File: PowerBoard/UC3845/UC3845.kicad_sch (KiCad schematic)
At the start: 41 parts, among them J1 AuxConn, J1 POWER_SW, Q1 STD11N65M2, U2 LT8316EFE#PBF

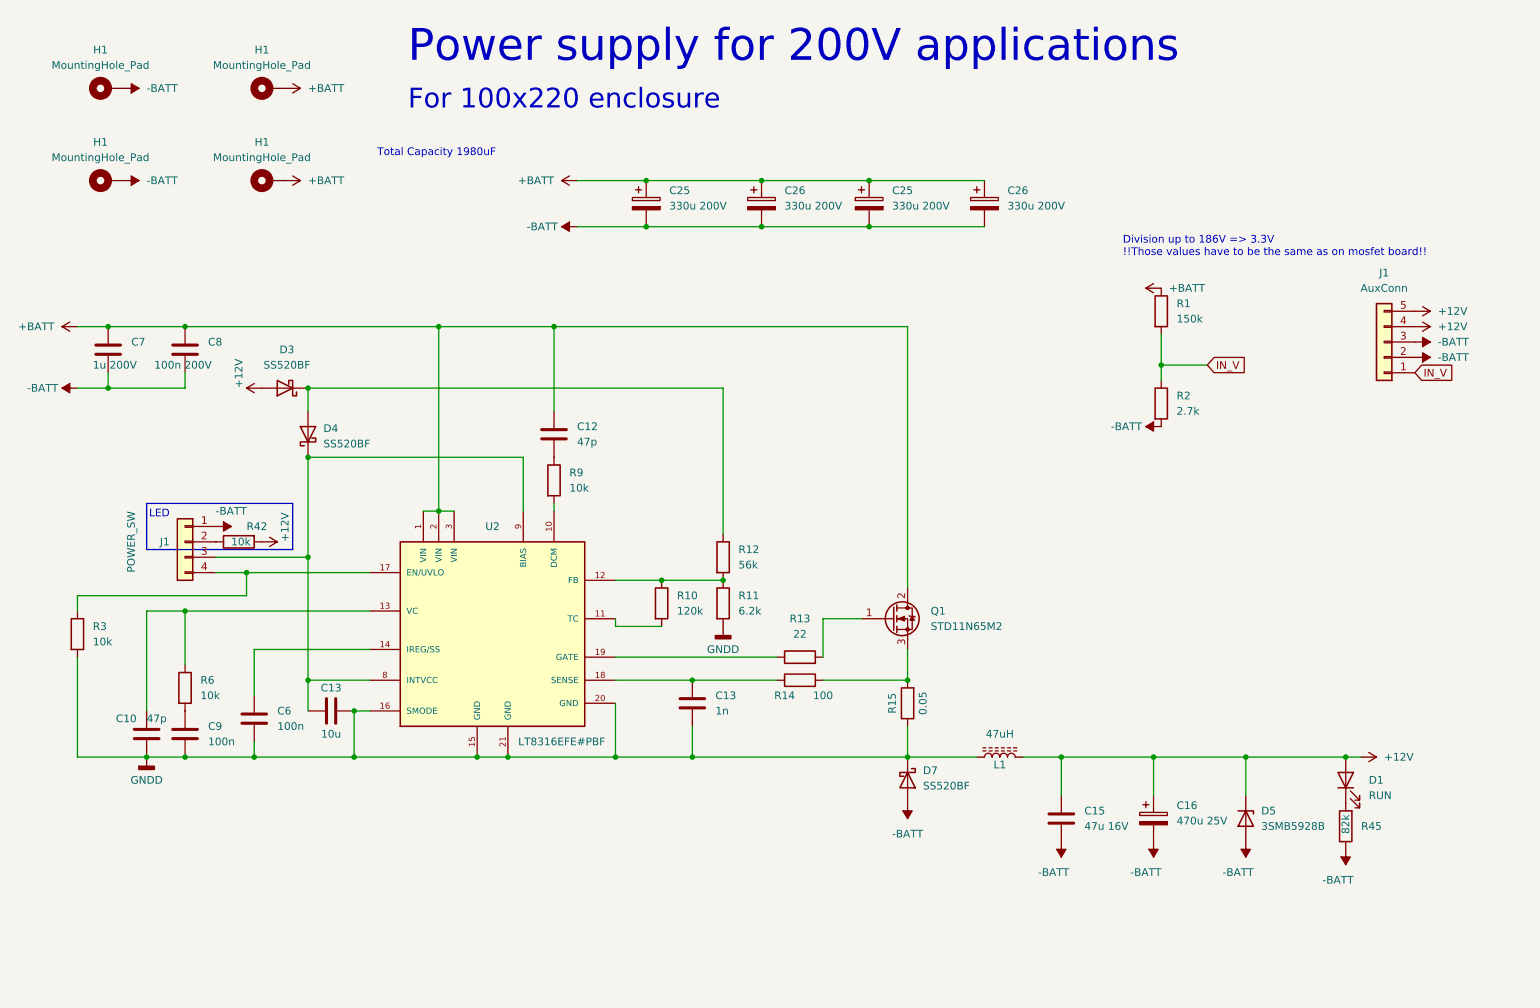
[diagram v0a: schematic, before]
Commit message: v3.0.1 - GaN redesign
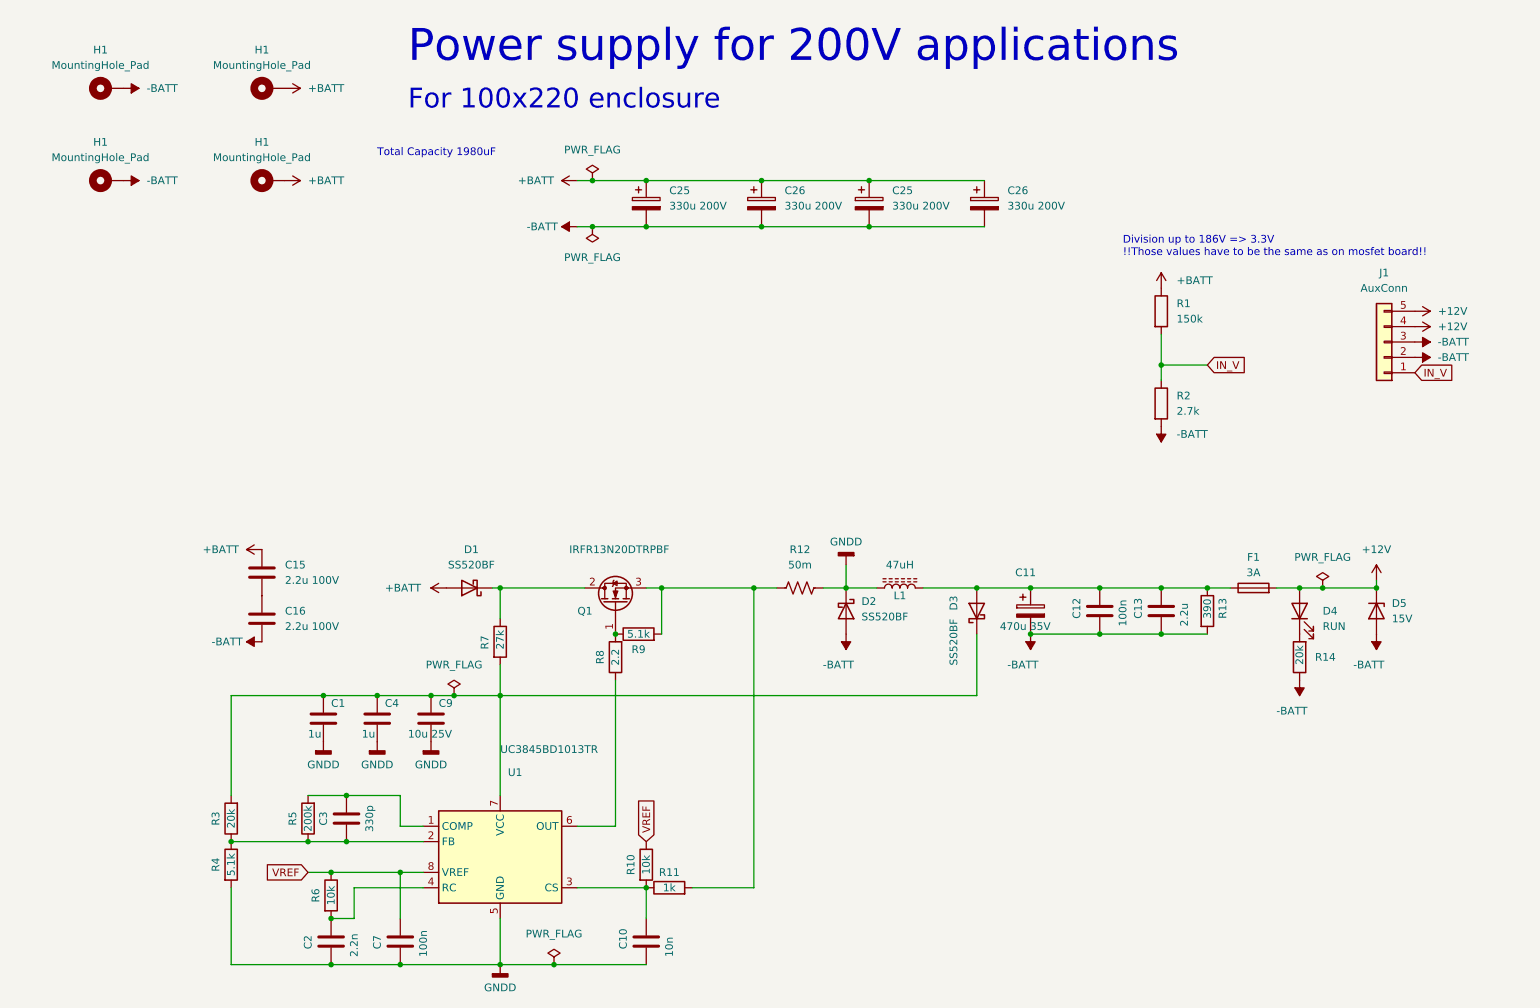
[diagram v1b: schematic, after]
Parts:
- removed C13: 1n, Capacitor_SMD:C_0603_1608Metric, symbol Device:C
- removed C13: 10u, Capacitor_SMD:C_0603_1608Metric, symbol Device:C
- removed C16: 470u 25V, Capacitor_SMD:CP_Elec_10x10.5, symbol Device:C_Polarized
- removed C6: 100n, GigaVescLibs:C_0603_1608Metric_L, symbol Device:C
- removed C8: 100n 200V, Capacitor_SMD:C_1206_3216Metric, symbol Device:C
- removed D1: RUN, Diode_SMD:D_0603_1608Metric, symbol Device:LED
- removed D4, D7: SS520BF, Diode_SMD:D_SMB, symbol Device:D_Schottky
- removed J1: POWER_SW, Connector_JST:JST_PH_B4B-PH-K_1x04_P2.00mm_Vertical, symbol Connector_Generic:Conn_01x04
- removed R12: 56k, Resistor_SMD:R_0603_1608Metric, symbol Device:R
- removed R15: 0.05, Resistor_SMD:R_2512_6332Metric, symbol Device:R
- removed R42: 10k, Resistor_SMD:R_0603_1608Metric, symbol Device:R
- removed R45: 82k, Resistor_SMD:R_0603_1608Metric, symbol Device:R
- removed U2: LT8316EFE#PBF, GigaVescLibs:IC_LT8316EFE#PBF, symbol GigaESCSymbols:LT8316EFE#PBF
- added C1, C4: 1u, Capacitor_SMD:C_0603_1608Metric, symbol Device:C
- added C11: 470u 35V, Capacitor_SMD:CP_Elec_10x10, symbol Device:C_Polarized
- added C13: 2.2u, Capacitor_SMD:C_0805_2012Metric, symbol Device:C
- added C16: 2.2u 100V, Capacitor_SMD:C_1206_3216Metric, symbol Device:C
- added C2: 2.2n, Capacitor_SMD:C_0603_1608Metric, symbol Device:C
- added C3: 330p, Capacitor_SMD:C_0603_1608Metric, symbol Device:C
- added D1, D2: SS520BF, Diode_SMD:D_SMB, symbol Device:D_Schottky
- added D4: RUN, Diode_SMD:D_0603_1608Metric, symbol Device:LED
- added F1: 3A, Fuse:Fuse_1206_3216Metric, symbol Device:Fuse
- added R12: 50m, Resistor_SMD:R_2512_6332Metric, symbol Device:R_US
- added R4: 5.1k, Resistor_SMD:R_0603_1608Metric, symbol Device:R
- added R5: 200k, Resistor_SMD:R_0603_1608Metric, symbol Device:R
- added R7: 27k, Resistor_SMD:R_0603_1608Metric, symbol Device:R
- added R8: 2.2, Resistor_SMD:R_0603_1608Metric, symbol Device:R
- added U1: UC3845BD1013TR, Package_SO:SOIC-8_3.9x4.9mm_P1.27mm, symbol Regulator_Controller:UC3842_SOIC8
- C10: value 47p -> 10n; footprint GigaVescLibs:C_0603_1608Metric_L -> Capacitor_SMD:C_0603_1608Metric; MPN C527044 -> C57112; Mouser 603-CC805JRNPO9BN470 -> 81-GRM55DR72D105KW1L
- C12: value 47p -> 100n; footprint GigaVescLibs:C_0603_1608Metric_L -> Capacitor_SMD:C_0603_1608Metric; MPN C527044 -> C14663; Mouser 80-C0603C470K1GAUTO -> 81-GRM55DR72D105KW1L
- C15: value 47u 16V -> 2.2u 100V; footprint Capacitor_SMD:C_1210_3225Metric -> Capacitor_SMD:C_1206_3216Metric; MPN C2918513 -> C920964; Mouser 81-GRM32EC81C476KE5K -> (none)
- C7: value 1u 200V -> 100n; footprint Capacitor_SMD:C_2220_5650Metric -> Capacitor_SMD:C_0603_1608Metric; MPN C78775 -> C14663
- C9: value 100n -> 10u 25V; footprint GigaVescLibs:C_0603_1608Metric_L -> Capacitor_SMD:C_0603_1608Metric; MPN C14663 -> C96446; Mouser 581-08055C104KAT4A -> (none)
- D5: value 3SMB5928B -> 15V; footprint Diode_SMD:D_SMB -> Diode_SMD:D_SMA; MPN C2983224 -> C110524; Mouser 821-1SMB5928 -> (none)
- J1: JLCPosOffset (none) -> -4,0; JLCRotOffset (none) -> 180
- Q1: value STD11N65M2 -> IRFR13N20DTRPBF; JLCPosOffset -1.27,0 -> 2,0; JLCRotOffset 0 -> 180; MPN C500947 -> C3021; Mouser 511-STD11N65M2 -> (none)
- R10: value 120k -> 10k; MPN C25808 -> C25804; Mouser 660-RK73H2ATTD1213F -> 603-AC0805JR-0710KL
- R11: value 6.2k -> 1k; MPN C4260 -> C4410; Mouser 667-ERJ-6ENF4991V -> (none)
- R13: value 22 -> 390; MPN C23345 -> C23151; Mouser 71-CRCW080520R0FKEAC -> (none)
- R14: value 100 -> 20k; MPN C22775 -> C4184; Mouser 791-WR08X1000FTL -> 603-AC0805JR-0710KL
- R3: value 10k -> 20k; MPN C25804 -> C4184; Mouser 756-WCR0603-10KFI -> (none)
- R9: value 10k -> 5.1k; MPN C25804 -> C23186; Mouser 756-WCR0603-10KFI -> (none)
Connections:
- net +12V: now also D4.2 (A), F1.2; no longer C15.1, D3.2 (A), L1.2
- net +BATT: now also C15.1, D1.2 (A); no longer C12.1, C7.1, Q1.2 (D)
- net -BATT: now also C12.2, R13.2, R14.1, C11.2, C13.2, C16.2, D2.2 (A); no longer C15.2, C7.2
- net GNDD: now also C7.2, C1.2, C2.2, C4.2, D2.1 (K), R12.2, R4.2, U1.5 (GND); no longer R11.2, R3.2
- net at D3.1 (K): now also C9.1, R3.2, C1.1, C4.1, R7.2, U1.7 (VCC)
- net at R13.1: now also C12.1, D3.2 (A), L1.2, C11.1, C13.1, F1.1
- net at Q1.1 (G): now also R9.1, R8.2; no longer R13.2
- net at R14.2: now also D4.1 (K); no longer Q1.3 (S)
- net at R3.1: now also C3.2, R4.1, R5.1, U1.2 (FB)
- net at R11.1: now also C10.1, R10.2, U1.3 (CS); no longer R10.1
- net at R6.2: now also C2.1, U1.4 (RC); no longer C9.1
- net at R9.2: now also Q1.3 (S), R11.2, R12.1
- net VREF: now reaches R6.1
- net VREF: now also C7.1, R10.1, U1.8 (VREF); no longer C10.1
- new net: C3.1, R5.2, U1.1 (COMP)
- new net: D1.1 (K), Q1.2 (D), R7.1
- new net: C15.2, C16.1
- new net: R8.1, U1.6 (OUT)
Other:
- note removed: "LED"
